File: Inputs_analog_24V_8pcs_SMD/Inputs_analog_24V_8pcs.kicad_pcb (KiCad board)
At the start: 2 copper layers, 115 parts, among them J1 Screw_Terminal_01x02, J10 Screw_Terminal_01x03, J11 Screw_Terminal_01x03, J2 Screw_Terminal_01x02, J3 Screw_Terminal_01x06, J4 Screw_Terminal_01x03, J5 Screw_Terminal_01x03, J6 Screw_Terminal_01x03, J7 Screw_Terminal_01x03, J8 Screw_Terminal_01x03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

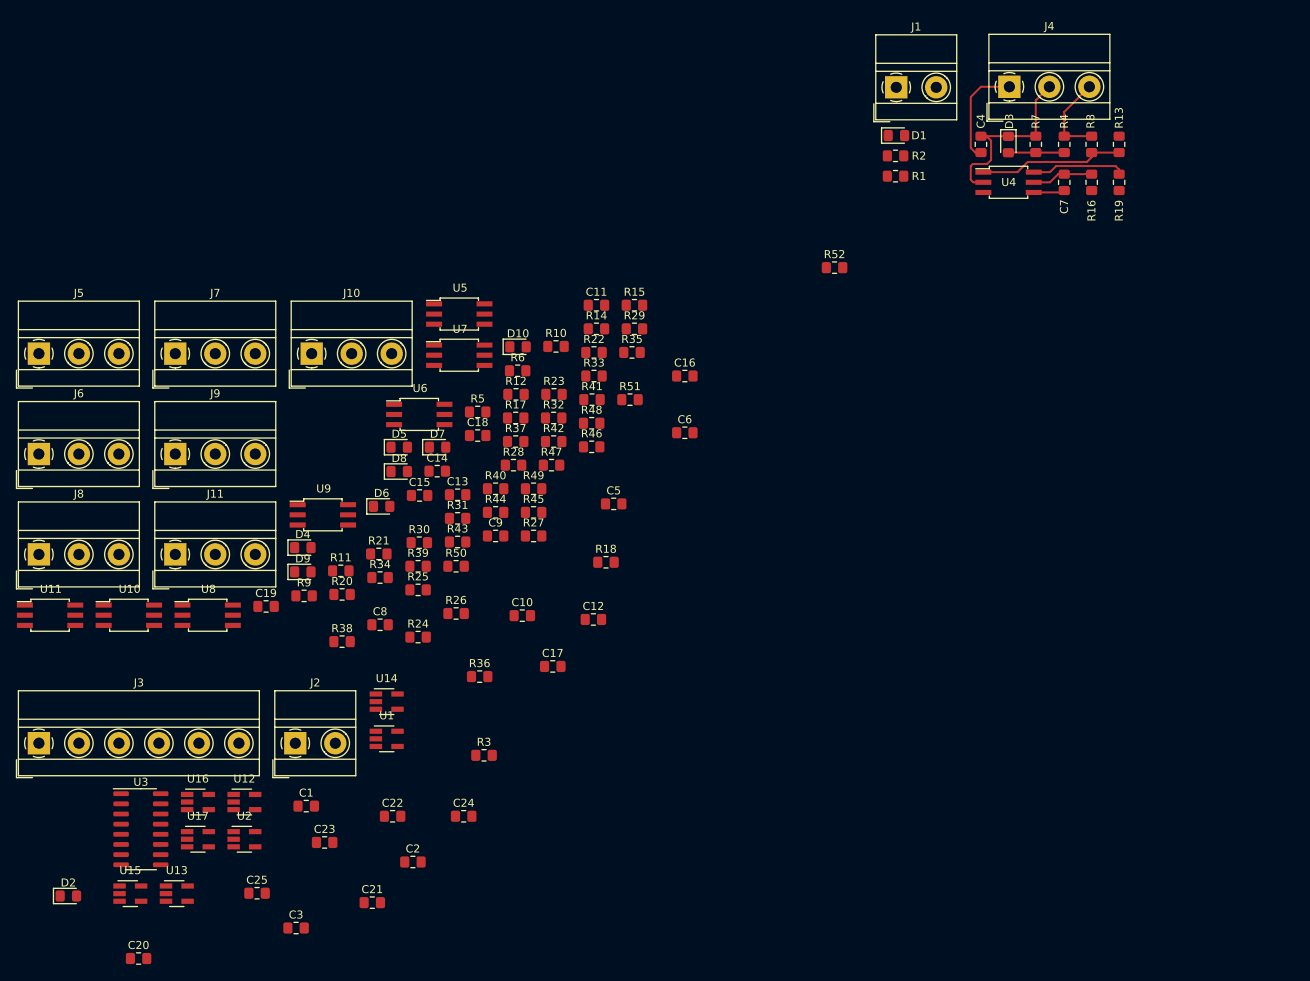
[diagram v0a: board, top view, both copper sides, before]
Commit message: Change footprints for ternimals
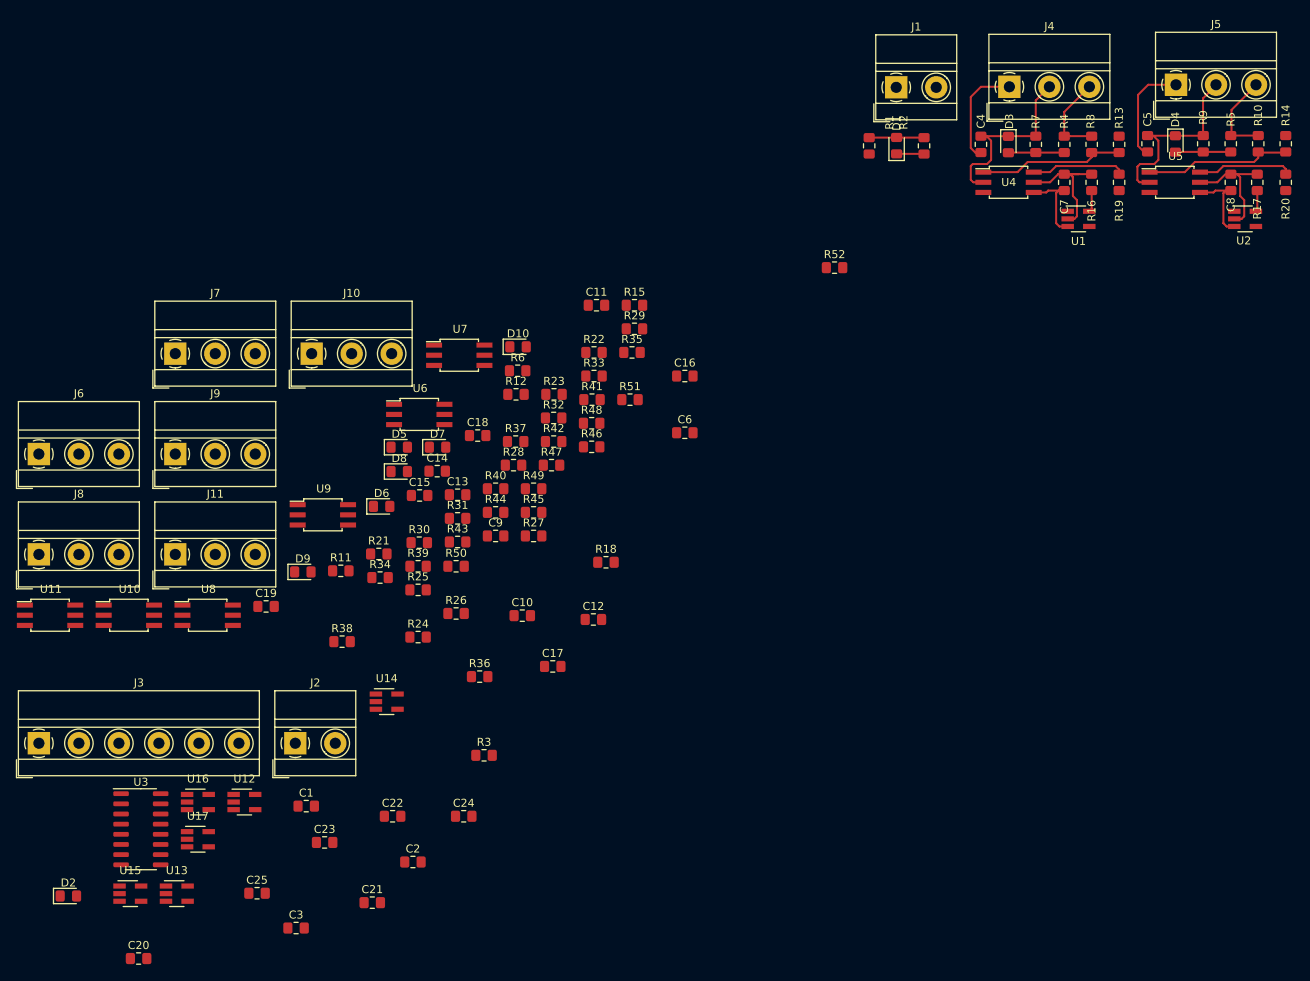
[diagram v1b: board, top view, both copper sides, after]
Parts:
- moved U2 147.2 mm to (66.5, 39.3)
- moved J5 146.1 mm to (57.8, 22.5)
- moved R20 128.7 mm to (71.5, 34.7), turned to 90 degrees
- moved R9 125.8 mm to (61.2, 29.9), turned to 270 degrees
- moved D4 120.2 mm to (57.8, 29.9), turned to 270 degrees
- moved C8 119.9 mm to (64.7, 34.7), turned to 270 degrees
- moved U1 108.2 mm to (45.6, 39.3)
- moved R5 99.9 mm to (64.7, 29.9), turned to 90 degrees
- moved R17 97.3 mm to (68.0, 34.7), turned to 90 degrees
- moved R10 91.4 mm to (68.1, 29.9), turned to 90 degrees
- moved U5 90.9 mm to (57.7, 34.7)
- moved R14 89.2 mm to (71.5, 29.9), turned to 90 degrees
- moved C5 80.5 mm to (54.3, 29.9), turned to 90 degrees
- moved R2 5.21 mm to (26.3, 30.2), turned to 90 degrees
- moved R1 3.52 mm to (19.5, 30.2), turned to 270 degrees
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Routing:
- net Earth: track 23.9 -> 50.7 mm
- net Net-(R10-Pad1): track 0.00 -> 18.4 mm
- net GND: track 3.91 -> 20.4 mm
- net input_2: track 0.00 -> 14.2 mm
- net +24V: track 13.2 -> 25.8 mm
- net Net-(R20-Pad2): track 0.00 -> 11.7 mm
- net Net-(J5-Pad3): track 0.00 -> 11.0 mm
- net input_1: track 7.66 -> 17.1 mm
- net Net-(D1-Pad2): track 0.00 -> 6.86 mm
- net Net-(D4-Pad2): track 0.00 -> 6.85 mm
- net +5V: track 0.00 -> 5.37 mm
